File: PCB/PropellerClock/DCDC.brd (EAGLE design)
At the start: 64 x 86 mm, 22 parts

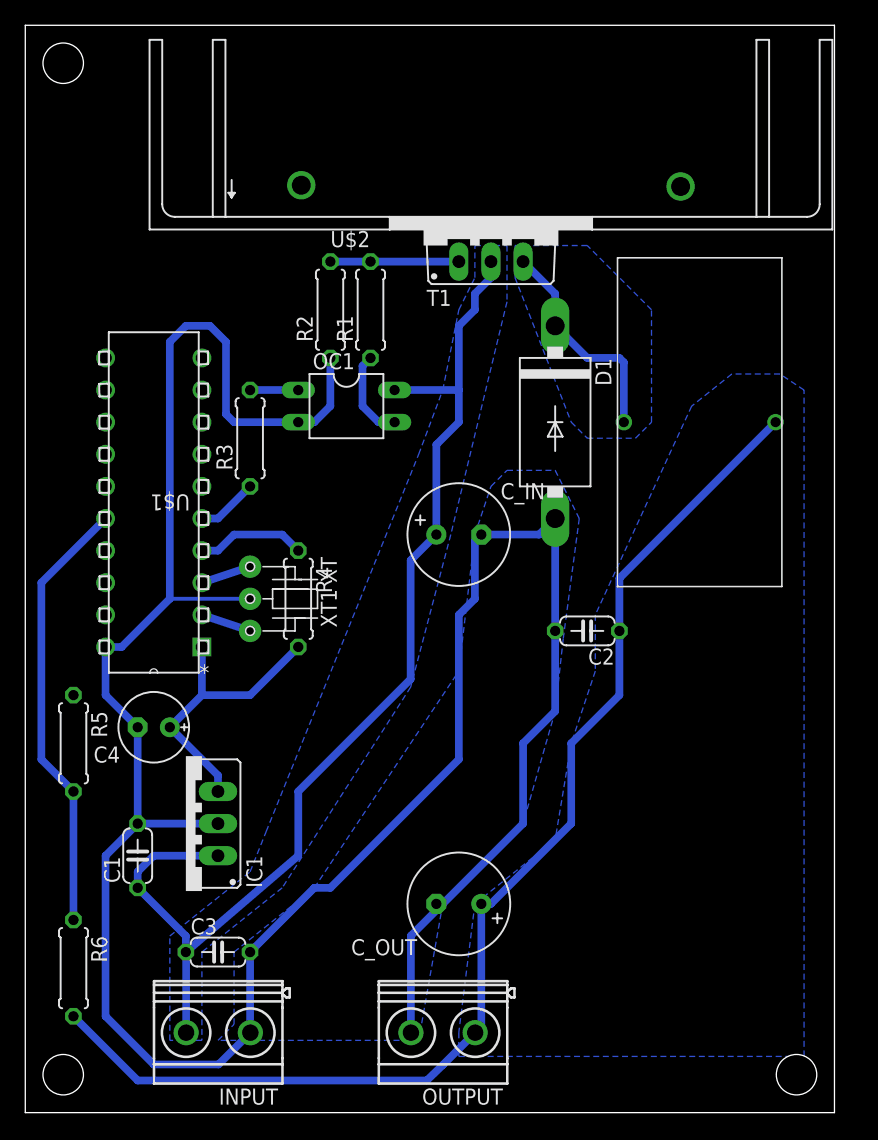
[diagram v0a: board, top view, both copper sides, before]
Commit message: デバックピン取り付け用の穴を追加 PICの入力保護用のツェナーダイオードを追加
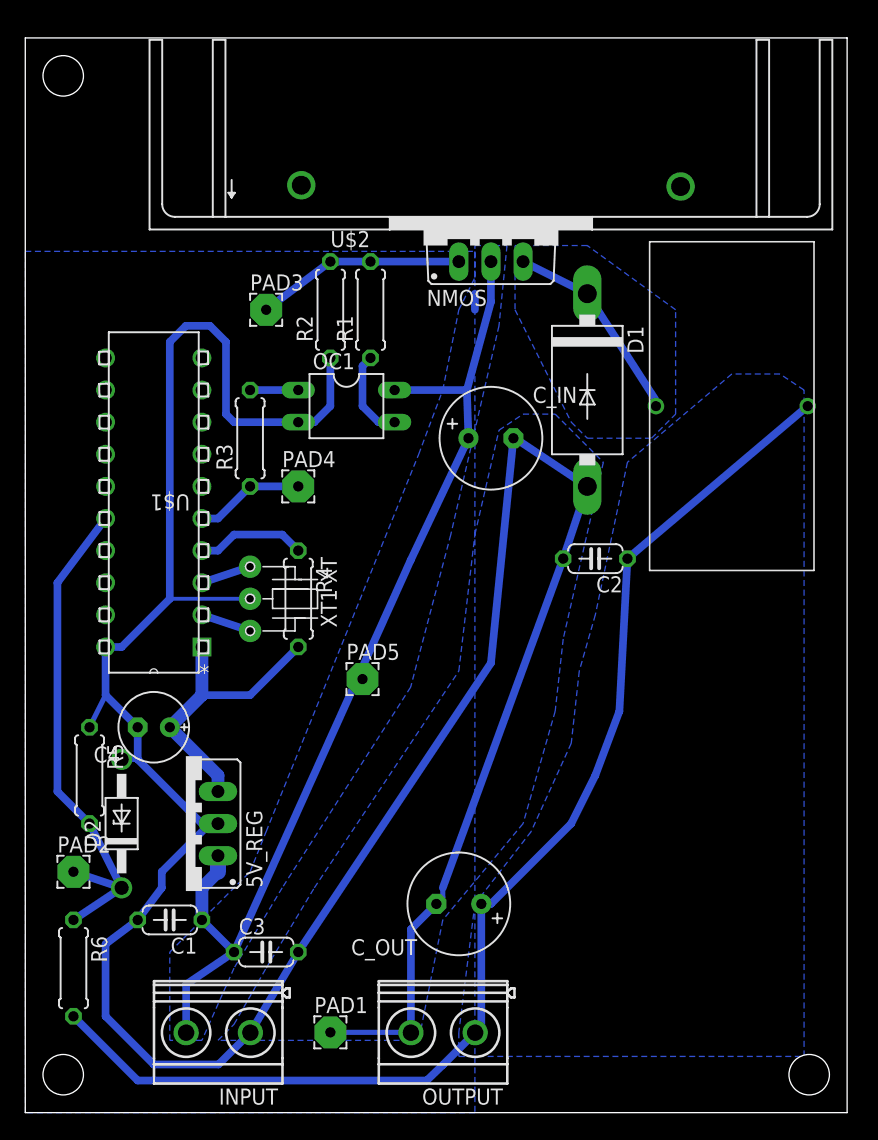
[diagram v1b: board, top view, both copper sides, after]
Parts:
- added D2: 1N4728, diode:DO41Z10
- added PAD1, PAD2, PAD3, PAD4, PAD5: (no value), wirepad:2,54/0,8
- R6: value 1k -> 2k
- moved C_IN 8.03 mm to (36.8, 53.3)
- moved C2 5.75 mm to (45.1, 43.8)
- moved C1 5.68 mm to (11.4, 15.2), turned to 180 degrees
- moved C3 3.81 mm to (19.1, 12.7)
- moved D1 3.59 mm to (44.5, 57.1)
- moved L1 2.84 mm to (55.9, 55.9)
- moved R5 2.84 mm to (5.08, 26.7)
- renumbered IC1 to 5V_REG, T1 to NMOS
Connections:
- removed net G_IN: NMOS.G, R1.2, R2.2
- new net GATE: NMOS.G, PAD3.1, R1.2, R2.2
- net +12V: now also PAD5.1
- net GND: now also D2.A, PAD1.1
- net S_OUT: now also PAD4.1
- net V_IN: now also D2.C, PAD2.1
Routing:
- net GATE: track 0.00 -> 16.5 mm
- net GND: track 209.2 -> 224.8 mm
- net G_IN: track 10.2 -> 0.00 mm
- net +12V: track 91.3 -> 83.5 mm
- net V_IN: track 34.9 -> 40.7 mm
- net S_OUT: track 4.86 -> 8.67 mm
- net V_OUT: track 94.0 -> 96.0 mm
- net N$7: track 17.5 -> 16.2 mm
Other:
- board size 64 x 86 mm -> 65 x 85 mm

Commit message: FETをNMOSからPMOSに変更
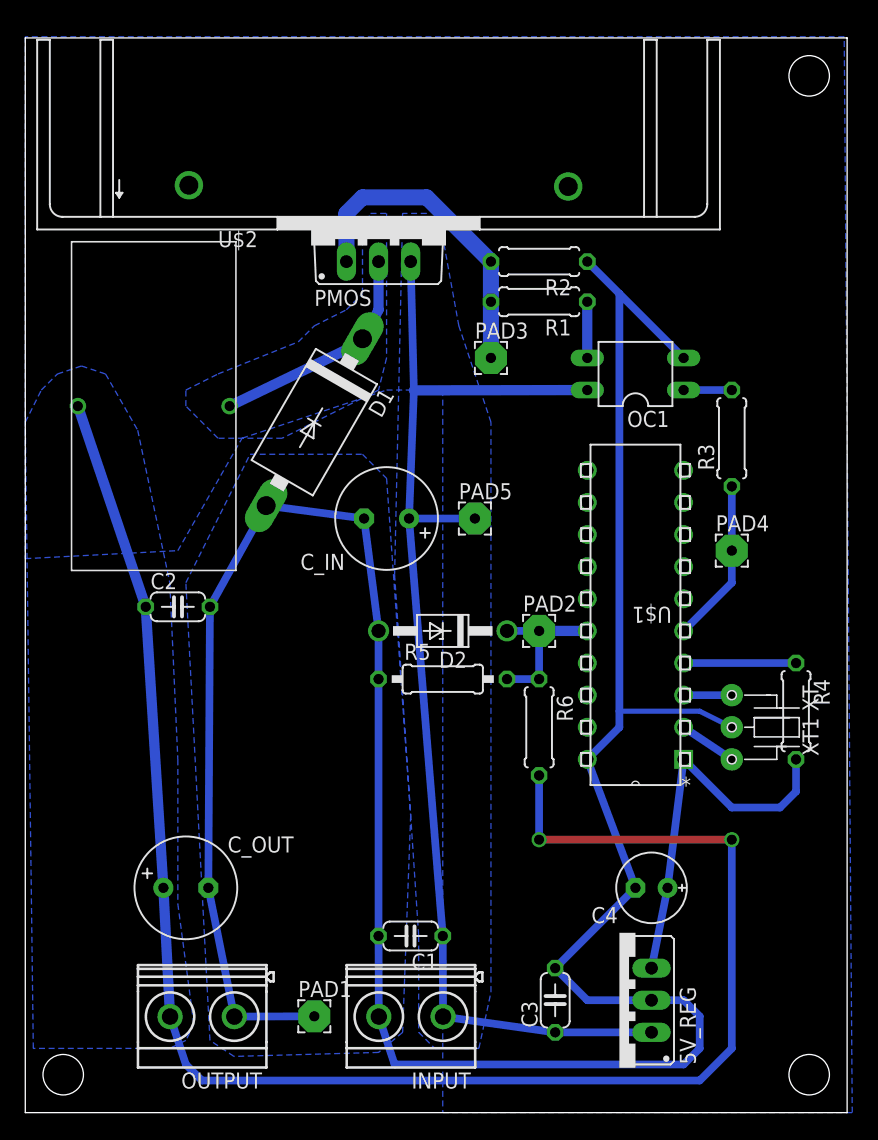
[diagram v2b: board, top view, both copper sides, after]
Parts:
- removed NMOS: (no value), transistor-power:TO220BV
- added PMOS: (no value), transistor-power:TO220BV
- R5: device rcl:0207/7 -> rcl:0207/10
- moved L1 45.7 mm to (10.2, 55.9), turned to 0 degrees
- moved PAD2 41.5 mm to (40.6, 38.1)
- moved R6 41.5 mm to (40.6, 30.5)
- moved C4 41.4 mm to (49.5, 17.8)
- moved R4 40.4 mm to (61.0, 31.8)
- moved XT1 39.4 mm to (59.7, 30.5)
- moved U$1 39.1 mm to (44.5, 50.8)
- moved R3 38.1 mm to (55.9, 53.3)
- moved 5V_REG 37.0 mm to (47.0, 8.89)
- moved PAD4 34.7 mm to (55.9, 44.5)
- moved C2 33.2 mm to (12.1, 40.0), turned to 0 degrees
- moved D2 29.6 mm to (33.0, 38.1), turned to 180 degrees
- moved R5 29.0 mm to (33.0, 34.3), turned to 0 degrees
- moved C3 23.2 mm to (41.9, 8.89), turned to 90 degrees
- moved OC1 23.0 mm to (48.3, 58.4), turned to 90 degrees
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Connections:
- net +12V: now also INPUT.1, PMOS.S; no longer INPUT.2, NMOS.D
- net GATE: now also PMOS.G; no longer NMOS.G
- net GND: now also INPUT.2, OUTPUT.1; no longer INPUT.1, OUTPUT.2
- net N$7: now also PMOS.D; no longer NMOS.S
- net V_OUT: now also OUTPUT.2; no longer OUTPUT.1
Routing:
- net V_OUT: track 96.0 -> 134.8 mm, vias 0 -> 2
- net V_IN: track 40.7 -> 12.7 mm
- net +12V: track 83.5 -> 95.3 mm
- net GATE: track 16.5 -> 25.5 mm
- net GND: track 224.8 -> 217.3 mm
- net +5V: track 23.3 -> 30.2 mm
- net S_OUT: track 8.67 -> 13.0 mm
- net N$2: track 7.14 -> 4.45 mm
- net N$7: track 16.2 -> 18.6 mm
- net N$4: track 4.02 -> 4.58 mm
